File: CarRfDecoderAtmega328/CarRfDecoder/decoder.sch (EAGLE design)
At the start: 53 parts, among them T1 BC847, T2 BC847, T3 IRLML6402, U2 RFM69CW, U3 MCP73831, U4 ATMEGA328P, U6 MIC5219 3.3V, Y1 16MHZ

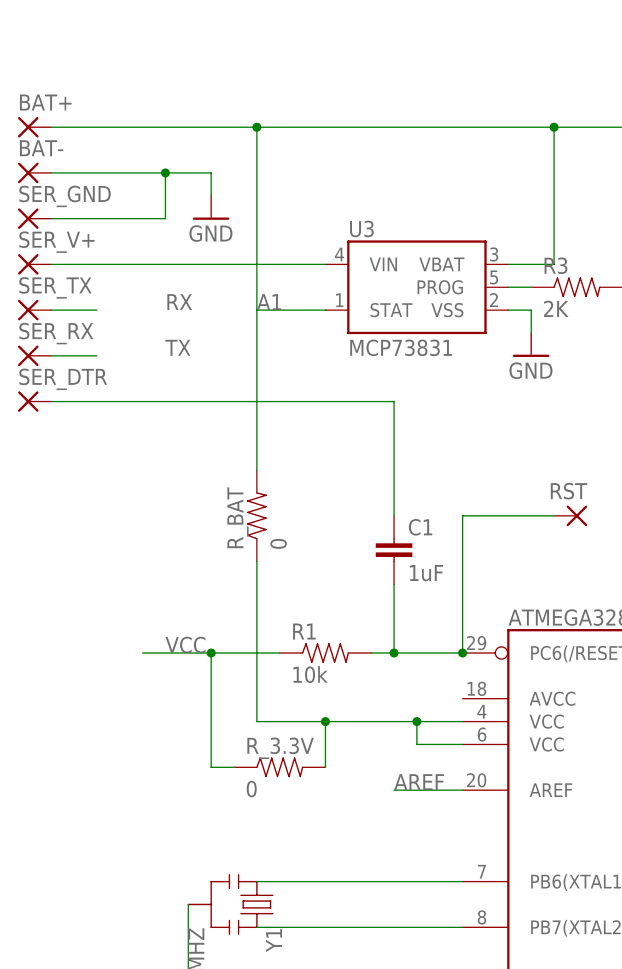
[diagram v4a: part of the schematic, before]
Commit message: Change the pin to H-bridge to allow reverse control of the motor using A5
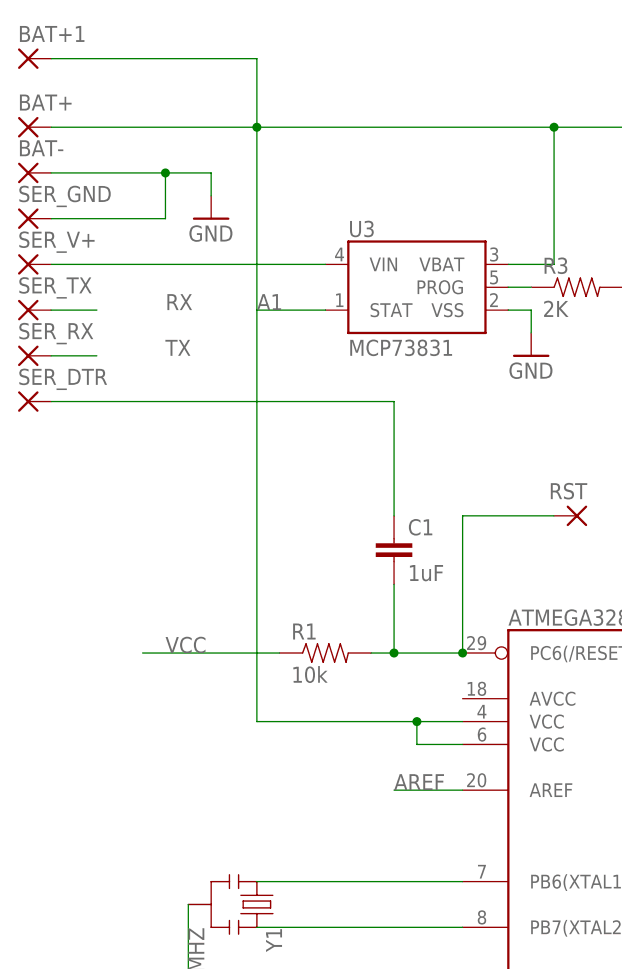
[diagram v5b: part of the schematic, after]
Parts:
- removed R_3.3V, R_BAT: 0, SparkFun-Resistors:RESISTOR0603-RES
- added BAT+1: (no value), wirepad:SMD2
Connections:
- removed net N$6: R_3.3V.2, R_BAT.1, U4.VCC@1, U4.VCC@2
- net BAT+: now also BAT+1.P, U4.VCC@1, U4.VCC@2; no longer R_BAT.2
- net VCC: no longer R_3.3V.1
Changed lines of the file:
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@@
 <part name="C1" library="SparkFun-Capacitors" deviceset="CAP" device="0805" value="1uF"/>
 <part name="RST" library="wirepad" deviceset="SMD2" device=""/>
-<part name="R_BAT" library="SparkFun-Resistors" deviceset="RESISTOR" device="0603-RES" value="0"/>
-<part name="R_3.3V" library="SparkFun-Resistors" deviceset="RESISTOR" device="0603-RES" value="0"/>
+<part name="BAT+1" library="wirepad" deviceset="SMD2" device=""/>
 </parts>
 <sheets>
@@
 <instance part="C1" gate="G$1" x="22.86" y="83.82"/>
 <instance part="RST" gate="1" x="43.18" y="88.9" rot="MR0"/>
-<instance part="R_BAT" gate="G$1" x="7.62" y="88.9" rot="R90"/>
-<instance part="R_3.3V" gate="G$1" x="10.16" y="60.96"/>
+<instance part="BAT+1" gate="1" x="-17.78" y="139.7"/>
 </instances>
 <busses>
@@
 <segment>
 <pinref part="R1" gate="G$1" pin="1"/>
-<wire x1="10.16" y1="73.66" x2="2.54" y2="73.66" width="0.1524" layer="91"/>
-<pinref part="R_3.3V" gate="G$1" pin="1"/>
-<wire x1="5.08" y1="60.96" x2="2.54" y2="60.96" width="0.1524" layer="91"/>
-<wire x1="2.54" y1="60.96" x2="2.54" y2="73.66" width="0.1524" layer="91"/>
-<wire x1="2.54" y1="73.66" x2="-5.08" y2="73.66" width="0.1524" layer="91"/>
-<junction x="2.54" y="73.66"/>
+<wire x1="10.16" y1="73.66" x2="-5.08" y2="73.66" width="0.1524" layer="91"/>
 <label x="-2.54" y="73.66" size="1.778" layer="95"/>
 </segment>
@@
 <pinref part="T3" gate="T" pin="S"/>
 <wire x1="205.74" y1="132.08" x2="205.74" y2="116.84" width="0.1524" layer="91"/>
-<pinref part="R_BAT" gate="G$1" pin="2"/>
-<wire x1="7.62" y1="93.98" x2="7.62" y2="132.08" width="0.1524" layer="91"/>
+<wire x1="7.62" y1="66.04" x2="7.62" y2="132.08" width="0.1524" layer="91"/>
 <junction x="7.62" y="132.08"/>
+<pinref part="BAT+1" gate="1" pin="P"/>
+<wire x1="-15.24" y1="139.7" x2="7.62" y2="139.7" width="0.1524" layer="91"/>
+<wire x1="7.62" y1="139.7" x2="7.62" y2="132.08" width="0.1524" layer="91"/>
+<pinref part="U4" gate="G$1" pin="VCC@2"/>
+<wire x1="25.4" y1="63.5" x2="30.48" y2="63.5" width="0.1524" layer="91"/>
+<pinref part="U4" gate="G$1" pin="VCC@1"/>
+<wire x1="30.48" y1="66.04" x2="25.4" y2="66.04" width="0.1524" layer="91"/>
+<wire x1="25.4" y1="66.04" x2="25.4" y2="63.5" width="0.1524" layer="91"/>
+<junction x="25.4" y="66.04"/>
+<wire x1="7.62" y1="66.04" x2="25.4" y2="66.04" width="0.1524" layer="91"/>
 </segment>
 </net>
@@
 </segment>
 </net>
-<net name="N$6" class="0">
-<segment>
-<pinref part="U4" gate="G$1" pin="VCC@2"/>
-<wire x1="25.4" y1="63.5" x2="30.48" y2="63.5" width="0.1524" layer="91"/>
-<pinref part="U4" gate="G$1" pin="VCC@1"/>
-<wire x1="30.48" y1="66.04" x2="25.4" y2="66.04" width="0.1524" layer="91"/>
-<wire x1="25.4" y1="66.04" x2="25.4" y2="63.5" width="0.1524" layer="91"/>
-<junction x="25.4" y="66.04"/>
-<wire x1="7.62" y1="66.04" x2="15.24" y2="66.04" width="0.1524" layer="91"/>
-<pinref part="R_BAT" gate="G$1" pin="1"/>
-<wire x1="15.24" y1="66.04" x2="25.4" y2="66.04" width="0.1524" layer="91"/>
-<wire x1="7.62" y1="66.04" x2="7.62" y2="83.82" width="0.1524" layer="91"/>
-<pinref part="R_3.3V" gate="G$1" pin="2"/>
-<wire x1="15.24" y1="66.04" x2="15.24" y2="60.96" width="0.1524" layer="91"/>
-<junction x="15.24" y="66.04"/>
-</segment>
-</net>

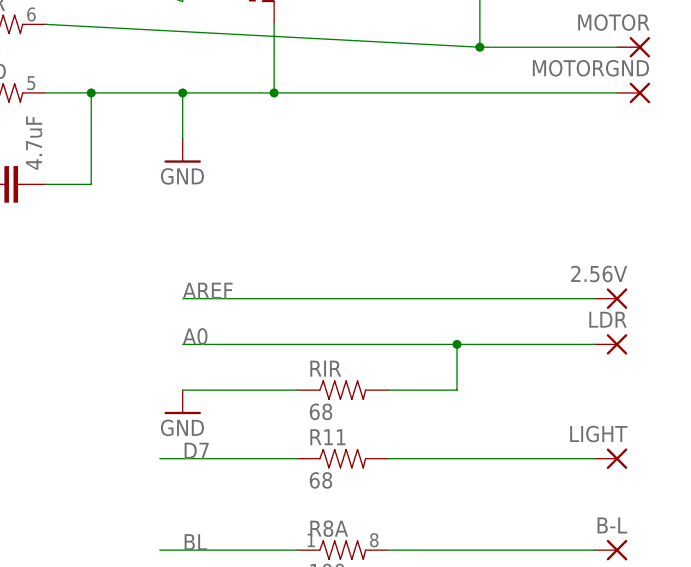
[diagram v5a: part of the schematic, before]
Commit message: New layout for RFM69HC
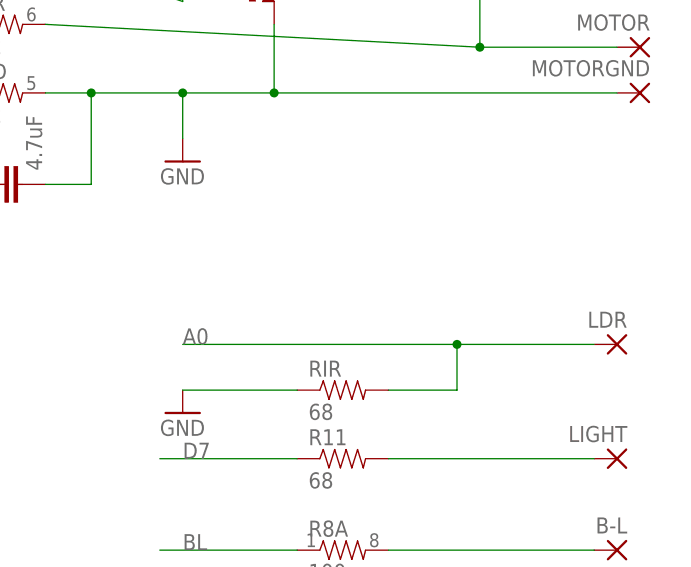
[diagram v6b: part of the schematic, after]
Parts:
- removed 2.56V: (no value), wirepad:SMD2
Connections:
- net AREF: no longer 2.56V.P
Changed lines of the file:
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@@
 <part name="R11" library="SparkFun-Resistors" deviceset="RESISTOR" device="0603-RES" value="68"/>
 <part name="LIGHT" library="wirepad" deviceset="SMD2" device=""/>
-<part name="2.56V" library="wirepad" deviceset="SMD2" device=""/>
 <part name="RIR" library="SparkFun-Resistors" deviceset="RESISTOR" device="0603-RES" value="68"/>
 <part name="LDR" library="wirepad" deviceset="SMD2" device=""/>
@@
 <instance part="R11" gate="G$1" x="190.5" y="50.8"/>
 <instance part="LIGHT" gate="1" x="220.98" y="50.8" rot="MR0"/>
-<instance part="2.56V" gate="1" x="220.98" y="68.58" rot="MR0"/>
 <instance part="RIR" gate="G$1" x="190.5" y="58.42"/>
 <instance part="LDR" gate="1" x="220.98" y="63.5" rot="MR0"/>
@@
 <net name="AREF" class="0">
 <segment>
-<wire x1="172.72" y1="68.58" x2="218.44" y2="68.58" width="0.1524" layer="91"/>
-<pinref part="2.56V" gate="1" pin="P"/>
-<label x="172.72" y="68.58" size="1.778" layer="95"/>
-</segment>
-<segment>
 <pinref part="U4" gate="G$1" pin="AREF"/>
